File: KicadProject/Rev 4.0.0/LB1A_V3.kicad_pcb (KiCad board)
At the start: 6 copper layers, 42 x 42 mm, 187 parts, among them J601 2337019-1, J602 2337019-1, U101 STM32MP157CAA3, U201 AS4C256M16D3LC-12BCN, U401 STPMIC1xPQR, U501 S40FC004C1B2C00000, U601 LBEE59B1LV-278, U701 DF40C-70DP-0.4V(51), U702 DF40C-100DP-0.4V(51), U703 DF40C-100DP-0.4V(51), X101 32.768kHz, Y101 24MHz

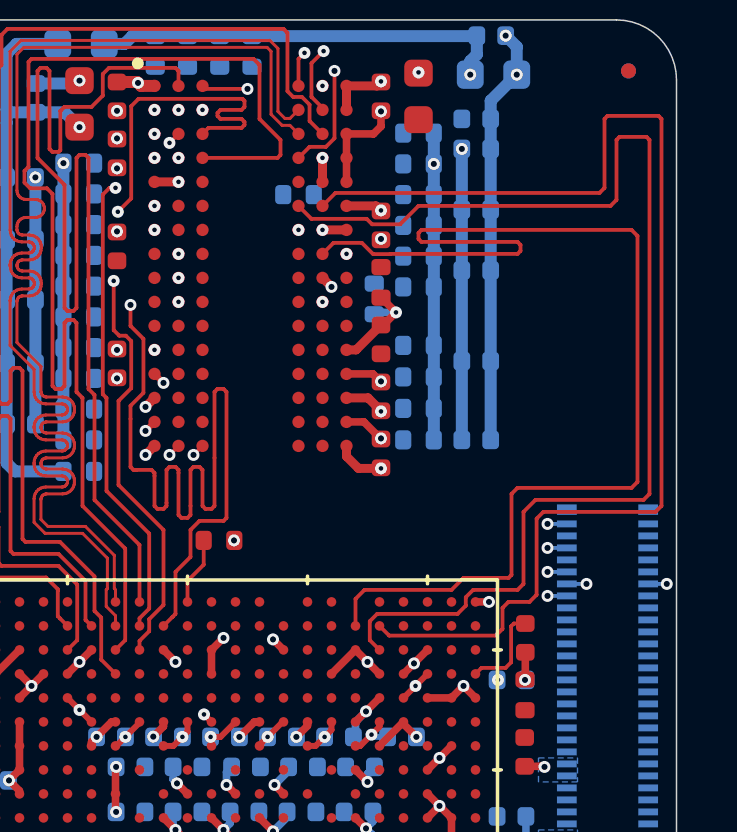
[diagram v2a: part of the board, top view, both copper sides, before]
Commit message: Updated ram routes
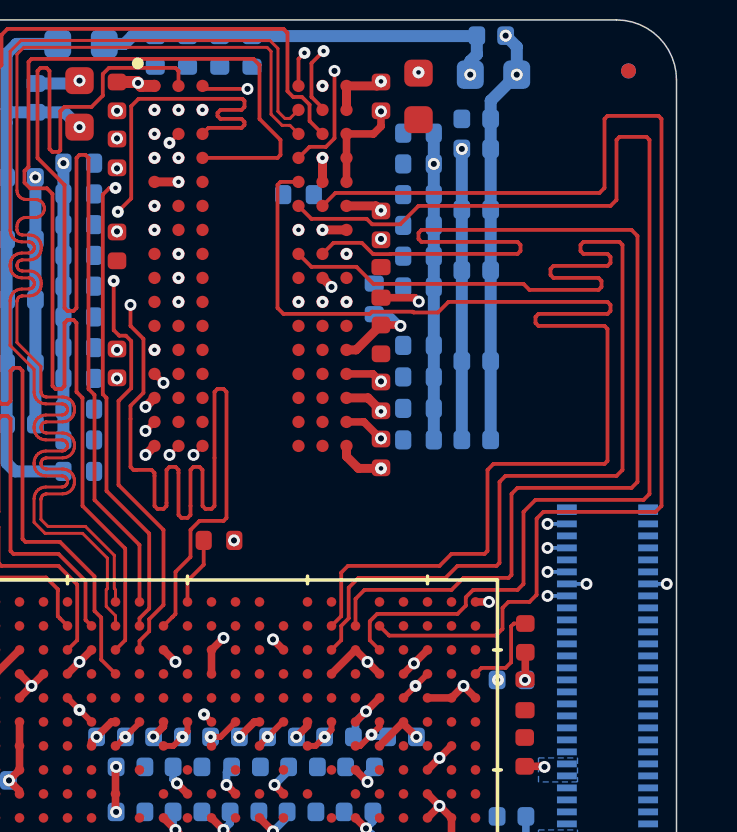
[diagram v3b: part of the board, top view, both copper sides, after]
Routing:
- net /MPU_DDR3L_Memory/DDR_DQM1: track 0.00 -> 40.0 mm
- net /MPU_DDR3L_Memory/DDR_DQ11: track 0.00 -> 40.0 mm
- net GND: track 203.0 -> 204.1 mm, vias 162 -> 163
- net /MPU_DDR3L_Memory/DDR_CLK_N: vias 0 -> 1
- net /MPU_DDR3L_Memory/DDR_CKE: vias 0 -> 1
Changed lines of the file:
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@@
     (thickness 1.2)
     (drawings 8)
-    (tracks 1652)
+    (tracks 1727)
     (zones 0)
     (modules 187)
@@
   (gr_arc (start 173 128) (end 171 128) (angle -90) (layer Edge.Cuts) (width 0.05))
   (gr_arc (start 173 90) (end 173 88) (angle -90) (layer Edge.Cuts) (width 0.05))
+  (via (at 202 97.4) (size 0.4) (drill 0.15) (layers L1_Sig_Pwr.Cu L6_Sig_Pwr.Cu) (net 58))
+  (via (at 200.4 97.4) (size 0.4) (drill 0.15) (layers L1_Sig_Pwr.Cu L6_Sig_Pwr.Cu) (net 62))
   (via (at 185.05 119.6) (size 0.4) (drill 0.15) (layers L1_Sig_Pwr.Cu L6_Sig_Pwr.Cu) (net 21))
   (via (at 207.05 110) (size 0.4) (drill 0.15) (layers L1_Sig_Pwr.Cu L6_Sig_Pwr.Cu) (net 9))
@@
   (via (at 207.305 88.525) (size 0.4) (drill 0.2) (layers L1_Sig_Pwr.Cu L6_Sig_Pwr.Cu) (net 1))
   (segment (start 203.15 98.17) (end 203.23 98.17) (width 0.254) (layer L1_Sig_Pwr.Cu) (net 1))
-  (via (at 203.65 97.75) (size 0.4) (drill 0.15) (layers L1_Sig_Pwr.Cu L6_Sig_Pwr.Cu) (net 1))
-  (segment (start 203.23 98.17) (end 203.65 97.75) (width 0.254) (layer L1_Sig_Pwr.Cu) (net 1))
   (segment (start 202.985 97.75) (end 202.925 97.81) (width 0.254) (layer L6_Sig_Pwr.Cu) (net 1))
-  (segment (start 203.65 97.75) (end 202.985 97.75) (width 0.254) (layer L6_Sig_Pwr.Cu) (net 1))
-  (segment (start 203.16 97.26) (end 203.65 97.75) (width 0.254) (layer L1_Sig_Pwr.Cu) (net 1))
   (segment (start 203.15 97.26) (end 203.16 97.26) (width 0.254) (layer L1_Sig_Pwr.Cu) (net 1))
   (segment (start 202 91) (end 202 90.2) (width 0.3) (layer L1_Sig_Pwr.Cu) (net 1))
@@
   (via (at 194.35 95.05) (size 0.4) (drill 0.2) (layers L1_Sig_Pwr.Cu L6_Sig_Pwr.Cu) (net 1))
   (via (at 194.35 99) (size 0.4) (drill 0.2) (layers L1_Sig_Pwr.Cu L6_Sig_Pwr.Cu) (net 1))
+  (via (at 203.8 98.2) (size 0.4) (drill 0.2) (layers L1_Sig_Pwr.Cu L6_Sig_Pwr.Cu) (net 1))
+  (segment (start 203.41 97.81) (end 203.8 98.2) (width 0.254) (layer L6_Sig_Pwr.Cu) (net 1))
+  (segment (start 202.925 97.81) (end 203.41 97.81) (width 0.254) (layer L6_Sig_Pwr.Cu) (net 1))
+  (segment (start 203.77 98.17) (end 203.8 98.2) (width 0.254) (layer L1_Sig_Pwr.Cu) (net 1))
+  (segment (start 203.15 98.17) (end 203.77 98.17) (width 0.254) (layer L1_Sig_Pwr.Cu) (net 1))
+  (via (at 204.41 97.389323) (size 0.4) (drill 0.2) (layers L1_Sig_Pwr.Cu L6_Sig_Pwr.Cu) (net 1))
+  (segment (start 204.280677 97.26) (end 204.41 97.389323) (width 0.254) (layer L1_Sig_Pwr.Cu) (net 1))
+  (segment (start 203.15 97.26) (end 204.280677 97.26) (width 0.254) (layer L1_Sig_Pwr.Cu) (net 1))
   (via (at 186.7 94.89) (size 0.4) (drill 0.15) (layers L1_Sig_Pwr.Cu L6_Sig_Pwr.Cu) (net 2))
   (segment (start 186.56 94.75) (end 186.7 94.89) (width 0.127) (layer L1_Sig_Pwr.Cu) (net 2))
@@
   (segment (start 185.15 94.3) (end 185.15 94.3865) (width 0.127) (layer L1_Sig_Pwr.Cu) (net 207))
   (segment (start 185 94.15) (end 185.15 94.3) (width 0.127) (layer L1_Sig_Pwr.Cu) (net 207))
+  (segment (start 200.831499 96.231499) (end 200.4 95.8) (width 0.127) (layer L1_Sig_Pwr.Cu) (net 221))
+  (segment (start 202.9 96.8) (end 202.331499 96.231499) (width 0.127) (layer L1_Sig_Pwr.Cu) (net 221))
+  (segment (start 210.4 97) (end 208.1 97) (width 0.127) (layer L1_Sig_Pwr.Cu) (net 221))
+  (segment (start 210.5 96.7) (end 210.5 96.9) (width 0.127) (layer L1_Sig_Pwr.Cu) (net 221))
+  (segment (start 211 103.2) (end 211.2 103) (width 0.127) (layer L1_Sig_Pwr.Cu) (net 221))
+  (segment (start 207.3 103.2) (end 211 103.2) (width 0.127) (layer L1_Sig_Pwr.Cu) (net 221))
+  (segment (start 210.8 96.1) (end 210.7 96.2) (width 0.127) (layer L1_Sig_Pwr.Cu) (net 221))
+  (segment (start 207.1 103.4) (end 207.3 103.2) (width 0.127) (layer L1_Sig_Pwr.Cu) (net 221))
+  (segment (start 208.8 96.5) (end 208.9 96.6) (width 0.127) (layer L1_Sig_Pwr.Cu) (net 221))
+  (segment (start 207.1 106.1) (end 207.1 103.4) (width 0.127) (layer L1_Sig_Pwr.Cu) (net 221))
+  (segment (start 205.7 106.2) (end 207 106.2) (width 0.127) (layer L1_Sig_Pwr.Cu) (net 221))
+  (segment (start 202.4 106.6) (end 205.3 106.6) (width 0.127) (layer L1_Sig_Pwr.Cu) (net 221))
+  (segment (start 207 106.2) (end 207.1 106.1) (width 0.127) (layer L1_Sig_Pwr.Cu) (net 221))
+  (segment (start 208.8 96.3) (end 208.8 96.5) (width 0.127) (layer L1_Sig_Pwr.Cu) (net 221))
+  (segment (start 202.07299 106.92701) (end 202.4 106.6) (width 0.127) (layer L1_Sig_Pwr.Cu) (net 221))
+  (segment (start 202.07299 107.948051) (end 202.07299 106.92701) (width 0.127) (layer L1_Sig_Pwr.Cu) (net 221))
+  (segment (start 201.823501 108.6765) (end 201.823501 108.19754) (width 0.127) (layer L1_Sig_Pwr.Cu) (net 221))
+  (segment (start 201.823501 108.19754) (end 202.07299 107.948051) (width 0.127) (layer L1_Sig_Pwr.Cu) (net 221))
+  (segment (start 207.9 96.8) (end 202.9 96.8) (width 0.127) (layer L1_Sig_Pwr.Cu) (net 221))
+  (segment (start 201.5 109.000001) (end 201.823501 108.6765) (width 0.127) (layer L1_Sig_Pwr.Cu) (net 221))
+  (segment (start 205.3 106.6) (end 205.7 106.2) (width 0.127) (layer L1_Sig_Pwr.Cu) (net 221))
+  (segment (start 211.2 103) (end 211.2 95.5) (width 0.127) (layer L1_Sig_Pwr.Cu) (net 221))
+  (segment (start 211.2 95.5) (end 211.1 95.4) (width 0.127) (layer L1_Sig_Pwr.Cu) (net 221))
+  (segment (start 210.8 95.9) (end 210.8 96.1) (width 0.127) (layer L1_Sig_Pwr.Cu) (net 221))
+  (segment (start 211.1 95.4) (end 209.9 95.4) (width 0.127) (layer L1_Sig_Pwr.Cu) (net 221))
+  (segment (start 209.9 95.4) (end 209.8 95.5) (width 0.127) (layer L1_Sig_Pwr.Cu) (net 221))
+  (segment (start 209.8 95.5) (end 209.8 95.7) (width 0.127) (layer L1_Sig_Pwr.Cu) (net 221))
+  (segment (start 209.8 95.7) (end 209.9 95.8) (width 0.127) (layer L1_Sig_Pwr.Cu) (net 221))
+  (segment (start 208.1 97) (end 207.9 96.8) (width 0.127) (layer L1_Sig_Pwr.Cu) (net 221))
+  (segment (start 209.9 95.8) (end 210.7 95.8) (width 0.127) (layer L1_Sig_Pwr.Cu) (net 221))
+  (segment (start 210.7 95.8) (end 210.8 95.9) (width 0.127) (layer L1_Sig_Pwr.Cu) (net 221))
+  (segment (start 202.331499 96.231499) (end 200.831499 96.231499) (width 0.127) (layer L1_Sig_Pwr.Cu) (net 221))
+  (segment (start 210.7 96.2) (end 208.9 96.2) (width 0.127) (layer L1_Sig_Pwr.Cu) (net 221))
+  (segment (start 208.9 96.2) (end 208.8 96.3) (width 0.127) (layer L1_Sig_Pwr.Cu) (net 221))
+  (segment (start 208.9 96.6) (end 210.4 96.6) (width 0.127) (layer L1_Sig_Pwr.Cu) (net 221))
+  (segment (start 210.5 96.9) (end 210.4 97) (width 0.127) (layer L1_Sig_Pwr.Cu) (net 221))
+  (segment (start 210.4 96.6) (end 210.5 96.7) (width 0.127) (layer L1_Sig_Pwr.Cu) (net 221))
+  (segment (start 199.7 93.5) (end 199.8 93.4) (width 0.127) (layer L1_Sig_Pwr.Cu) (net 222))
+  (segment (start 199.7 97.6) (end 199.7 93.5) (width 0.127) (layer L1_Sig_Pwr.Cu) (net 222))
+  (segment (start 210.6 102.8) (end 210.7 102.7) (width 0.127) (layer L1_Sig_Pwr.Cu) (net 222))
+  (segment (start 210.8 97.5) (end 210.7 97.4) (width 0.127) (layer L1_Sig_Pwr.Cu) (net 222))
+  (segment (start 205.1 106.2) (end 205.5 105.8) (width 0.127) (layer L1_Sig_Pwr.Cu) (net 222))
+  (segment (start 210.7 98.3) (end 210.6 98.2) (width 0.127) (layer L1_Sig_Pwr.Cu) (net 222))
+  (segment (start 210.7 102.7) (end 210.7 98.3) (width 0.127) (layer L1_Sig_Pwr.Cu) (net 222))
+  (segment (start 210.6 98.2) (end 208.4 98.2) (width 0.127) (layer L1_Sig_Pwr.Cu) (net 222))
+  (segment (start 205.5 105.8) (end 206.6 105.8) (width 0.127) (layer L1_Sig_Pwr.Cu) (net 222))
+  (segment (start 202.047002 106.2) (end 205.1 106.2) (width 0.127) (layer L1_Sig_Pwr.Cu) (net 222))
+  (segment (start 202.85428 97.72649) (end 202.78077 97.8) (width 0.127) (layer L1_Sig_Pwr.Cu) (net 222))
+  (segment (start 201.823501 106.423501) (end 202.047002 106.2) (width 0.127) (layer L1_Sig_Pwr.Cu) (net 222))
+  (segment (start 210.8 97.7) (end 210.8 97.5) (width 0.127) (layer L1_Sig_Pwr.Cu) (net 222))
+  (segment (start 201.823501 107.8765) (end 201.823501 106.423501) (width 0.127) (layer L1_Sig_Pwr.Cu) (net 222))
+  (segment (start 199.9 97.8) (end 199.7 97.6) (width 0.127) (layer L1_Sig_Pwr.Cu) (net 222))
+  (segment (start 206.9 102.8) (end 210.6 102.8) (width 0.127) (layer L1_Sig_Pwr.Cu) (net 222))
+  (segment (start 206.7 105.7) (end 206.7 103) (width 0.127) (layer L1_Sig_Pwr.Cu) (net 222))
+  (segment (start 206.7 103) (end 206.9 102.8) (width 0.127) (layer L1_Sig_Pwr.Cu) (net 222))
+  (segment (start 205.4 97.4) (end 205.047176 97.752824) (width 0.127) (layer L1_Sig_Pwr.Cu) (net 222))
+  (segment (start 199.8 93.4) (end 200.4 93.4) (width 0.127) (layer L1_Sig_Pwr.Cu) (net 222))
+  (segment (start 201.5 108.200001) (end 201.823501 107.8765) (width 0.127) (layer L1_Sig_Pwr.Cu) (net 222))
+  (segment (start 208.4 98.2) (end 208.3 98.1) (width 0.127) (layer L1_Sig_Pwr.Cu) (net 222))
+  (segment (start 208.3 98.1) (end 208.3 97.9) (width 0.127) (layer L1_Sig_Pwr.Cu) (net 222))
+  (segment (start 208.3 97.9) (end 208.4 97.8) (width 0.127) (layer L1_Sig_Pwr.Cu) (net 222))
+  (segment (start 208.4 97.8) (end 210.7 97.8) (width 0.127) (layer L1_Sig_Pwr.Cu) (net 222))
+  (segment (start 206.6 105.8) (end 206.7 105.7) (width 0.127) (layer L1_Sig_Pwr.Cu) (net 222))
+  (segment (start 210.7 97.8) (end 210.8 97.7) (width 0.127) (layer L1_Sig_Pwr.Cu) (net 222))
+  (segment (start 210.7 97.4) (end 205.4 97.4) (width 0.127) (layer L1_Sig_Pwr.Cu) (net 222))
+  (segment (start 205.047176 97.752824) (end 204.235519 97.752824) (width 0.127) (layer L1_Sig_Pwr.Cu) (net 222))
+  (segment (start 204.235519 97.752824) (end 204.209185 97.72649) (width 0.127) (layer L1_Sig_Pwr.Cu) (net 222))
+  (segment (start 204.209185 97.72649) (end 202.85428 97.72649) (width 0.127) (layer L1_Sig_Pwr.Cu) (net 222))
+  (segment (start 202.78077 97.8) (end 199.9 97.8) (width 0.127) (layer L1_Sig_Pwr.Cu) (net 222))
   (segment (start 202.6 107) (end 202.3 107.3) (width 0.127) (layer L1_Sig_Pwr.Cu) (net 231))
   (segment (start 205.5 107) (end 202.6 107) (width 0.127) (layer L1_Sig_Pwr.Cu) (net 231))

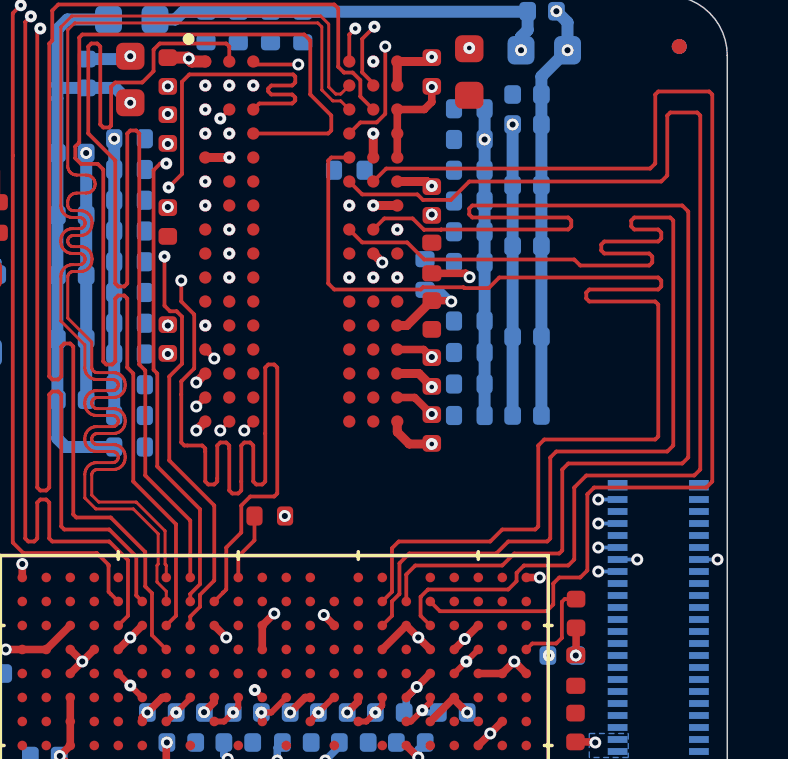
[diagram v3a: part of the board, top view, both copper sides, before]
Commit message: differential clock in ram routed
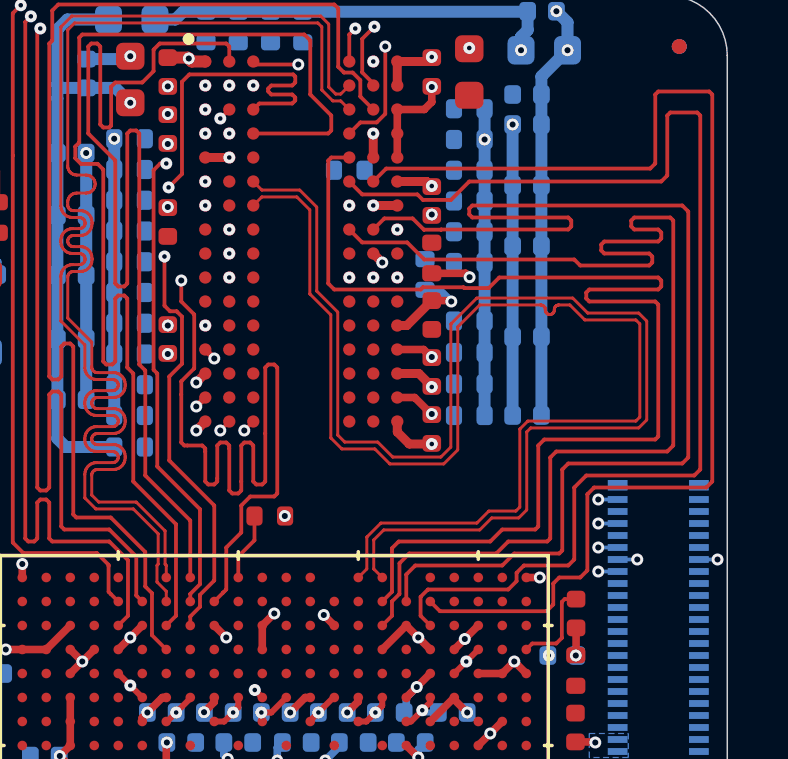
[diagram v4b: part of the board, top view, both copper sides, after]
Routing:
- net /MPU_DDR3L_Memory/DDR_DQS1_N: track 0.00 -> 42.8 mm
- net /MPU_DDR3L_Memory/DDR_DQS1_P: track 0.00 -> 42.8 mm

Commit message: one more trace left
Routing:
- net /MPU_DDR3L_Memory/DDR_DQ13: track 0.00 -> 40.1 mm, vias 0 -> 2
- net /MPU_DDR3L_Memory/DDR_DQ9: track 0.00 -> 40.1 mm
- net /MPU_DDR3L_Memory/DDR_DQ10: track 0.00 -> 40.0 mm, vias 0 -> 2
- net /MPU_DDR3L_Memory/DDR_DQ8: track 0.00 -> 0.90 mm, vias 0 -> 1
